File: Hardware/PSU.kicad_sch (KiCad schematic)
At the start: 29 parts

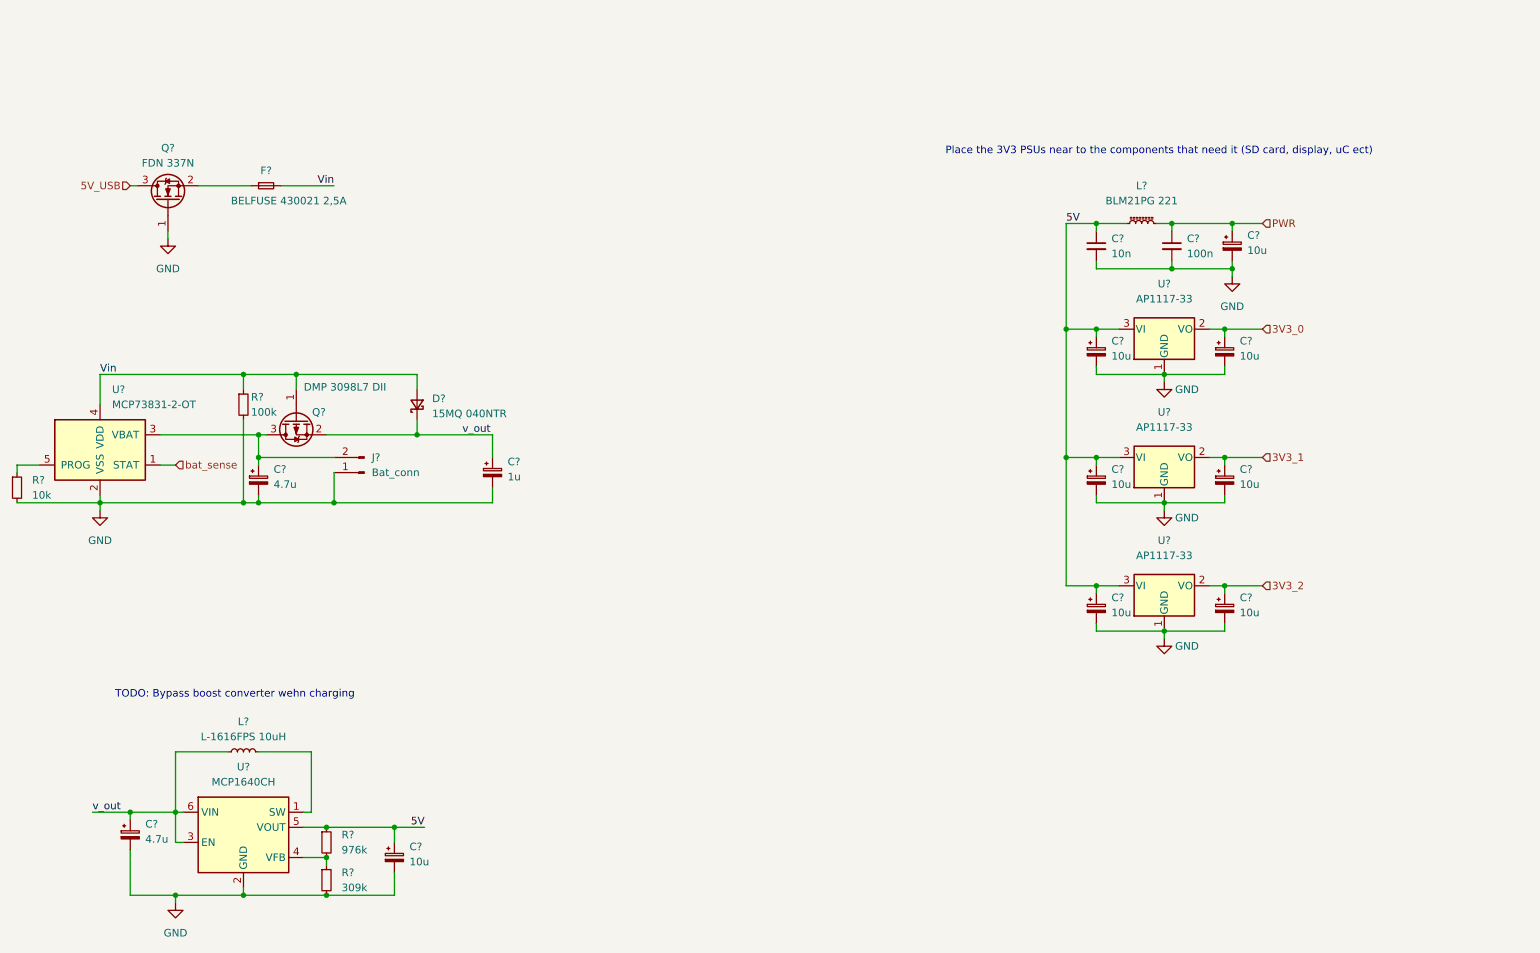
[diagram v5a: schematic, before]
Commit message: added buttons and stuff
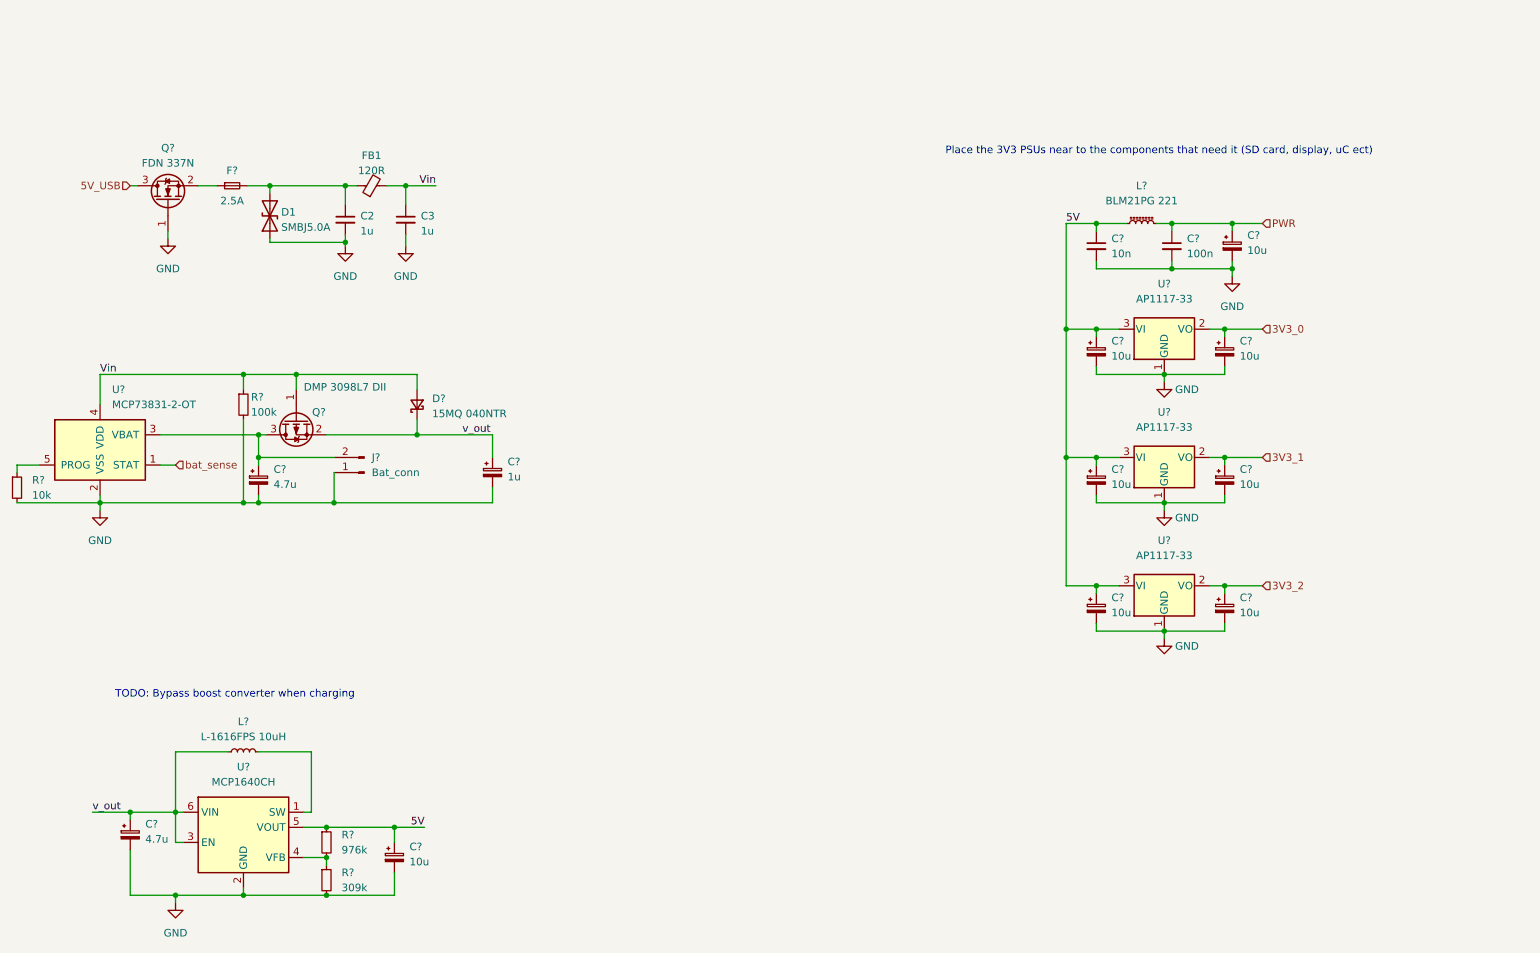
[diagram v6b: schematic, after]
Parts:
- added C2, C3: 1u, symbol Device:C_Small
- added D1: SMBJ5.0A, symbol Device:D_TVS
- added FB1: 120R, symbol Device:FerriteBead_Small
- F?: value BELFUSE 430021 2,5A -> 2.5A
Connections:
- net GND: now also C2.2, C3.2, D1.1 (A1)
- net Vin: now also C3.1, FB1.2; no longer F?.2
- new net: C2.1, D1.2 (A2), F?.2, FB1.1
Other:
- note added: "TODO: Bypass boost converter when charging"
- note removed: "TODO: Bypass boost converter wehn charging"
- moved on the sheet: F?
